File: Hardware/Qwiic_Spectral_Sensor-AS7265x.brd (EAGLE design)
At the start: 35.6 x 40.6 mm, 93 parts, among them J2 Serial Interface, J5 Flash Programming, J8 PTH, U1 AS72651, U3 4MB Flash, U5 AS72653, U6 AS72652

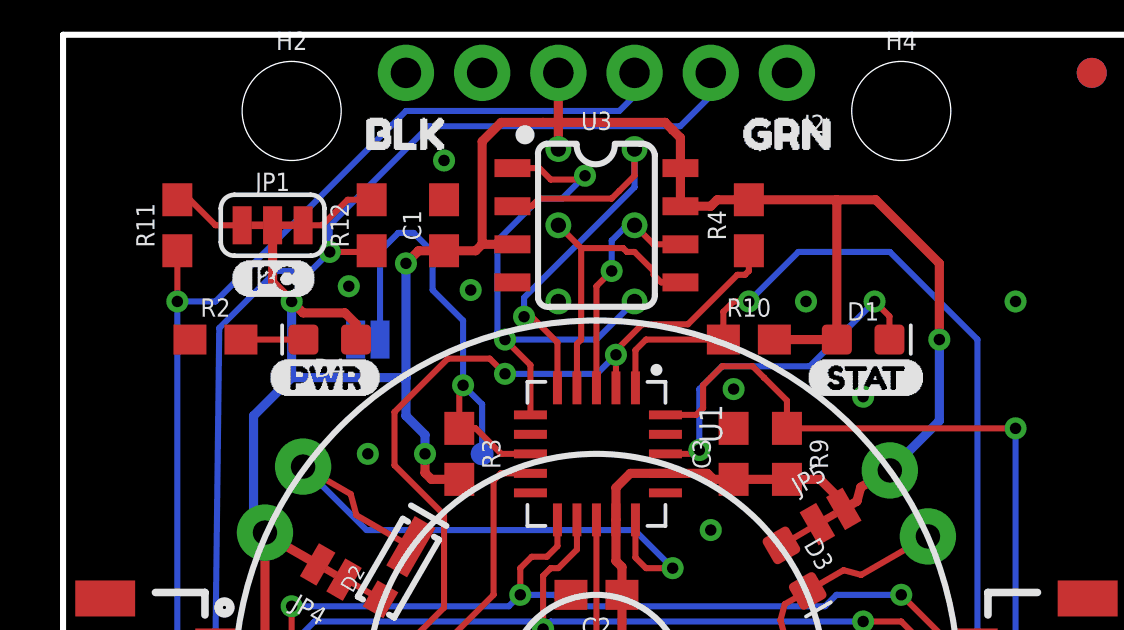
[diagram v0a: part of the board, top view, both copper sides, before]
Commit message: Adding LED disconnect jumpers
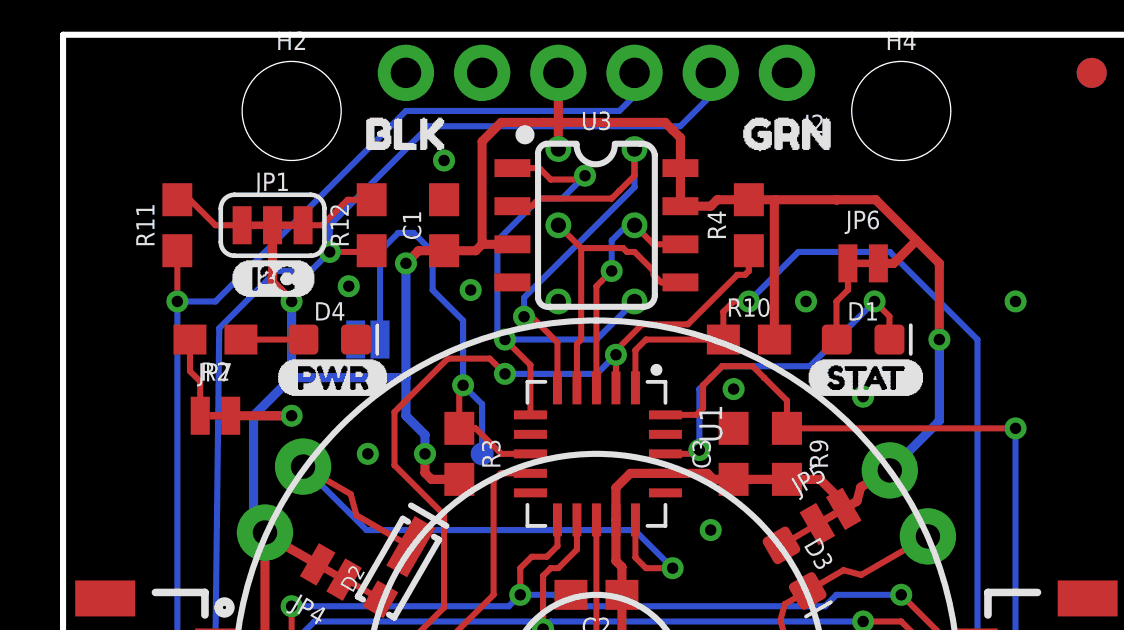
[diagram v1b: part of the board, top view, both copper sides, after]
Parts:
- added JP6, JP7: (no value), SparkFun-Jumpers:SMT-JUMPER_2_NC_TRACE_NO-SILK
- moved U$3 0.25 mm to (7.11, 29.2)
- turned D4 to 0 degrees
- turned R2 to 180 degrees
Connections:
- new net N$10: D1.A, JP6.1
- new net N$7: D4.A, R2.1
- net 3.3V: now also JP6.2, JP7.2; no longer D1.A, D4.A
- net GND: now also D4.C; no longer R2.1
- net N$1: now also JP7.1; no longer D4.C
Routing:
- net N$10: track 0.00 -> 2.70 mm
- net N$7: track 0.00 -> 2.08 mm
- net N$1: track 2.08 -> 2.68 mm
- net 3.3V: track 143.3 -> 143.2 mm, vias 4 -> 5
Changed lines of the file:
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@@
 <attribute name="NAME" x="7.62" y="4.572" size="0.6096" layer="25" font="vector" ratio="20" align="bottom-center"/>
 </element>
-<element name="D4" library="SparkFun-LED" package="LED-0603" value="RED" x="8.89" y="30.48" smashed="yes" rot="R180">
-<attribute name="NAME" x="8.89" y="29.845" size="0.6096" layer="25" font="vector" ratio="20" rot="R180" align="bottom-center"/>
-<attribute name="PROD_ID" value="DIO-00819" x="8.89" y="30.48" size="1.778" layer="27" font="vector" ratio="15" rot="R180" display="off"/>
-<attribute name="VALUE" x="8.89" y="31.115" size="0.6096" layer="27" font="vector" ratio="20" rot="R180" align="top-center"/>
+<element name="D4" library="SparkFun-LED" package="LED-0603" value="RED" x="8.89" y="30.48" smashed="yes">
+<attribute name="NAME" x="8.89" y="31.115" size="0.6096" layer="25" font="vector" ratio="20" align="bottom-center"/>
+<attribute name="PROD_ID" value="DIO-00819" x="8.89" y="30.48" size="1.778" layer="27" font="vector" ratio="15" display="off"/>
+<attribute name="VALUE" x="8.89" y="29.845" size="0.6096" layer="27" font="vector" ratio="20" align="top-center"/>
 </element>
-<element name="R2" library="SparkFun-Resistors" package="0603" value="1k" x="5.08" y="30.48" smashed="yes">
-<attribute name="NAME" x="5.08" y="31.242" size="0.6096" layer="25" font="vector" ratio="20" align="bottom-center"/>
-<attribute name="PROD_ID" value="RES-07856" x="5.08" y="30.48" size="1.778" layer="27" font="vector" ratio="15" display="off"/>
-<attribute name="VALUE" x="5.08" y="29.718" size="0.6096" layer="27" font="vector" ratio="20" align="top-center"/>
+<element name="R2" library="SparkFun-Resistors" package="0603" value="1k" x="5.08" y="30.48" smashed="yes" rot="R180">
+<attribute name="NAME" x="5.08" y="29.718" size="0.6096" layer="25" font="vector" ratio="20" rot="R180" align="bottom-center"/>
+<attribute name="PROD_ID" value="RES-07856" x="5.08" y="30.48" size="1.778" layer="27" font="vector" ratio="15" rot="R180" display="off"/>
+<attribute name="VALUE" x="5.08" y="31.242" size="0.6096" layer="27" font="vector" ratio="20" rot="R180" align="top-center"/>
 </element>
 <element name="U$2" library="Labels" package="I_SUPER2_C-()-03" value="" x="5.588" y="32.512" smashed="yes"/>
-<element name="U$3" library="Labels" package="PWR-()-03" value="" x="6.858" y="29.21" smashed="yes"/>
+<element name="U$3" library="Labels" package="PWR-()-03" value="" x="7.112" y="29.21" smashed="yes"/>
 <element name="U$4" library="buzzard_labels (50)" package="AS7265X0" value="" x="0.254" y="9.779" smashed="yes"/>
 <element name="U$5" library="buzzard_labels (50)" package="BULB15" value="" x="10.414" y="26.543" smashed="yes" rot="MR300"/>
@@
 <element name="U$39" library="buzzard_labels (7)" package="#1" value="" x="6.985" y="28.575" smashed="yes" rot="MR300"/>
 <element name="U$40" library="buzzard_labels (7)" package="#1" value="" x="30.988" y="23.749" smashed="yes" rot="MR60"/>
+<element name="JP6" library="SparkFun-Jumpers" package="SMT-JUMPER_2_NC_TRACE_NO-SILK" value="" x="26.67" y="33.02" smashed="yes">
+<attribute name="NAME" x="26.67" y="34.163" size="0.6096" layer="25" font="vector" ratio="20" align="bottom-center"/>
+<attribute name="VALUE" x="26.67" y="31.877" size="0.6096" layer="27" font="vector" ratio="20" align="top-center"/>
+</element>
+<element name="JP7" library="SparkFun-Jumpers" package="SMT-JUMPER_2_NC_TRACE_NO-SILK" value="" x="5.08" y="27.94" smashed="yes">
+<attribute name="NAME" x="5.08" y="29.083" size="0.6096" layer="25" font="vector" ratio="20" align="bottom-center"/>
+<attribute name="VALUE" x="5.08" y="26.797" size="0.6096" layer="27" font="vector" ratio="20" align="top-center"/>
+</element>
 </elements>
 <signals>
@@
 <via x="30.48" y="15.24" extent="1-16" drill="0.381"/>
 <via x="9.525" y="32.258" extent="1-16" drill="0.381"/>
-<contactref element="R2" pad="1"/>
 <via x="12.7" y="8.89" extent="1-16" drill="0.381"/>
 <via x="5.08" y="12.7" extent="1-16" drill="0.381"/>
@@
 <via x="33.655" y="19.05" extent="1-16" drill="0.381"/>
 <via x="24.765" y="31.75" extent="1-16" drill="0.381"/>
+<contactref element="D4" pad="C"/>
 </signal>
 <signal name="RX/SCL">
@@
 <contactref element="U3" pad="7"/>
 <contactref element="U3" pad="3"/>
-<contactref element="D1" pad="A"/>
 <contactref element="C3" pad="1"/>
 <contactref element="J1" pad="2"/>
@@
 <wire x1="20.58" y1="36.194953125" x2="20.5799875" y2="37.20495" width="0.3048" layer="1"/>
 <wire x1="20.5799875" y1="37.20495" x2="20.319996875" y2="37.464946875" width="0.3048" layer="1"/>
-<wire x1="25.792975" y1="30.479965625" x2="23.709990625" y2="30.479959375" width="0.3048" layer="1"/>
 <wire x1="26.4642625" y1="25.0903875" x2="26.024321875" y2="24.8363875" width="0.3048" layer="1"/>
 <wire x1="26.589921875" y1="25.559346875" x2="26.4642625" y2="25.0903875" width="0.3048" layer="1"/>
@@
 <wire x1="29.21" y1="30.48" x2="29.21" y2="27.76986875" width="0.3048" layer="16"/>
 <wire x1="29.21" y1="27.76986875" x2="27.558959375" y2="26.118828125" width="0.3048" layer="16"/>
-<wire x1="25.792975" y1="35.127975" x2="25.792975" y2="30.479965625" width="0.3048" layer="1"/>
-<wire x1="25.781" y1="35.13995" x2="22.859990625" y2="35.13995" width="0.3048" layer="1"/>
+<wire x1="25.781" y1="35.13995" x2="23.749" y2="35.13995" width="0.3048" layer="1"/>
+<wire x1="23.749" y1="35.13995" x2="22.859990625" y2="35.13995" width="0.3048" layer="1"/>
 <wire x1="27.09005" y1="35.13995" x2="25.781" y2="35.13995" width="0.3048" layer="1"/>
-<wire x1="29.21" y1="33.02" x2="27.09005" y2="35.13995" width="0.3048" layer="1"/>
+<wire x1="29.21" y1="33.02" x2="28.448" y2="33.782" width="0.3048" layer="1"/>
+<wire x1="28.448" y1="33.782" x2="27.09005" y2="35.13995" width="0.3048" layer="1"/>
 <wire x1="29.21" y1="33.02" x2="29.21" y2="30.48" width="0.3048" layer="1"/>
 <via x="12.065" y="26.67" extent="1-16" drill="0.381"/>
@@
 <wire x1="25.2340375" y1="25.8199625" x2="24.12996875" y2="25.8199625" width="0.3048" layer="1"/>
 <wire x1="26.024321875" y1="25.029678125" x2="25.2340375" y2="25.8199625" width="0.3048" layer="1"/>
-<contactref element="D4" pad="A"/>
 <wire x1="7.62" y1="31.75" x2="6.985" y2="32.385" width="0.3048" layer="1"/>
 <via x="7.62" y="31.75" extent="1-16" drill="0.381"/>
 <wire x1="7.62" y1="31.75" x2="7.62" y2="29.21" width="0.3048" layer="16"/>
-<wire x1="9.767" y1="31" x2="9.767" y2="30.48" width="0.3048" layer="1"/>
-<wire x1="9.767" y1="31" x2="9.398" y2="31.369" width="0.3048" layer="1"/>
-<wire x1="9.398" y1="31.369" x2="8.001" y2="31.369" width="0.3048" layer="1"/>
-<wire x1="8.001" y1="31.369" x2="7.62" y2="31.75" width="0.3048" layer="1"/>
 <wire x1="6.731028125" y1="24.046115625" x2="6.731028125" y2="24.004896875" width="0.3048" layer="1"/>
 <wire x1="6.746115625" y1="23.989809375" x2="6.731028125" y2="24.004896875" width="0.3048" layer="1"/>
@@
 <wire x1="26.024321875" y1="25.029678125" x2="26.024321875" y2="24.8363875" width="0.3048" layer="1"/>
 <wire x1="6.985" y1="34.29" x2="6.985" y2="32.385" width="0.3048" layer="1"/>
+<contactref element="JP7" pad="2"/>
+<contactref element="JP6" pad="2"/>
+<wire x1="5.588" y1="27.94" x2="7.62" y2="27.94" width="0.3048" layer="1"/>
+<via x="7.62" y="27.94" extent="1-16" drill="0.381"/>
+<wire x1="7.62" y1="27.94" x2="6.35" y2="27.94" width="0.3048" layer="16"/>
+<wire x1="27.178" y1="33.02" x2="27.686" y2="33.02" width="0.3048" layer="1"/>
+<wire x1="27.686" y1="33.02" x2="28.448" y2="33.782" width="0.3048" layer="1"/>
+<wire x1="23.709990625" y1="30.479959375" x2="23.709990625" y2="35.100940625" width="0.3048" layer="1"/>
+<wire x1="23.709990625" y1="35.100940625" x2="23.749" y2="35.13995" width="0.3048" layer="1"/>
 </signal>
 <signal name="!RST">
@@
 </signal>
 <signal name="N$1">
-<contactref element="D4" pad="C"/>
 <contactref element="R2" pad="2"/>
-<wire x1="8.013" y1="30.48" x2="5.93" y2="30.48" width="0.2032" layer="1"/>
+<contactref element="JP7" pad="1"/>
+<wire x1="4.572" y1="27.94" x2="4.572" y2="29.083" width="0.2032" layer="1"/>
+<wire x1="4.23" y1="29.425" x2="4.23" y2="30.48" width="0.2032" layer="1"/>
+<wire x1="4.572" y1="29.083" x2="4.23" y2="29.425" width="0.2032" layer="1"/>
+</signal>
+<signal name="N$7">
+<contactref element="D4" pad="A"/>
+<contactref element="R2" pad="1"/>
+<wire x1="5.93" y1="30.48" x2="8.013" y2="30.48" width="0.2032" layer="1"/>
+</signal>
+<signal name="N$10">
+<contactref element="D1" pad="A"/>
+<contactref element="JP6" pad="1"/>
+<wire x1="26.162" y1="33.02" x2="26.162" y2="32.131" width="0.2032" layer="1"/>
+<wire x1="26.162" y1="32.131" x2="25.781" y2="31.75" width="0.2032" layer="1"/>
+<wire x1="25.781" y1="31.75" x2="25.781" y2="30.491940625" width="0.2032" layer="1"/>
+<wire x1="25.781" y1="30.491940625" x2="25.792975" y2="30.479965625" width="0.2032" layer="1"/>
 </signal>
 </signals>

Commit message: Commit before panels
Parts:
- removed JP6: (no value), SparkFun-Jumpers:SMT-JUMPER_2_NC_TRACE_NO-SILK
- removed U6: AS72652, Qwiic_Spectral_Sensor-AS7265x:LGA20
- added U2: 4MB Flash, SparkFun-IC-Memory:SO08
- U3: value 4MB Flash -> AS72652; device SparkFun-IC-Memory:SO08 -> Qwiic_Spectral_Sensor-AS7265x:LGA20
- moved U3 20.2 mm to (24.4, 15.2), turned to 60 degrees
- renumbered U5 to U4
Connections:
- removed net N$10: D1.A, JP6.1
- net !CS_EE: now also U2.1; no longer U3.1
- net !RST-ADDR: now also U3.2; no longer U6.2
- net 3.3V: now also D1.A, U2.3, U2.7, U2.8, U3.14, U3.17; no longer JP6.2, U3.3, U3.7, U3.8, U6.14, U6.17
- net GND: now also U2.4, U3.16; no longer U3.4, U6.16
- net LED_DRV1: now also U3.15; no longer U6.15
- net MISO: now also U2.2; no longer U3.2
- net MOSI: now also U2.5; no longer U3.5
- net N$3: now also U3.7; no longer U6.7
- net N$9: now also U3.5; no longer U6.5
- net SCK: now also U2.6; no longer U3.6
- net SCL_S: now also U3.9; no longer U6.9
- net SDA_S: now also U3.10; no longer U6.10
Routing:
- net N$10: track 2.70 -> 0.00 mm
- net 3.3V: track 143.2 -> 144.2 mm
- net SDA_S: track 56.9 -> 57.5 mm
